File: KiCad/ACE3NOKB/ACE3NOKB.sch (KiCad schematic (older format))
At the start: 92 parts, among them J5 Conn_01x08_Female, J6 Conn_01x05_Female, J7 Conn_01x03, J8 Conn_02x05, Q1 2N3904, Q101 2N3904, Q2 2N2369, X1 6.5MHz

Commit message: Semi Complete KEyboard interface.
Signed-off-by: John Bradley <flypie@rocketmail.com>
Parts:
- Z0: Manufacturer_Part_Number Z84C0020PEG -> Z84C0020VEG
- Z101: value SN74ALS21AN -> SN74AS21N; Manufacturer_Part_Number SN74ALS21AN -> SN74AS21N
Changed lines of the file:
@@
 F 3 "" H 2925 7025 50  0001 C CNN
 F 4 "Zilog" H 400 525 50  0001 C CNN "Manufacturer_Name"
-F 5 "Z84C0020PEG" H 400 525 50  0001 C CNN "Manufacturer_Part_Number"
+F 5 "Z84C0020VEG" H 400 525 50  0001 C CNN "Manufacturer_Part_Number"
 	1    2925 6875
 	1    0    0    -1
@@
 P 11475 15275
 F 0 "Z101" H 11750 15325 50  0000 L CNN
-F 1 "SN74ALS21AN" H 11750 15275 50  0000 L CNN
+F 1 "SN74AS21N" H 11750 15275 50  0000 L CNN
 F 2 "Package_DIP:DIP-14_W7.62mm" H 11475 15275 50  0001 C CNN
 F 3 "http://www.ti.com/lit/gpn/sn74LS21" H 11475 15275 50  0001 C CNN
-F 4 "SN74ALS21AN " H 11475 15275 50  0001 C CNN "Manufacturer_Part_Number"
+F 4 "SN74AS21N" H 11475 15275 50  0001 C CNN "Manufacturer_Part_Number"
 F 5 "Texas Instruments" H 11475 15275 50  0001 C CNN "Manufacturer_Name"
 	3    11475 15275
@@
 P 6750 6075
 F 0 "Z101" H 6750 6475 50  0000 C CNN
-F 1 "SN74ALS21AN" H 6750 6375 50  0000 C CNN
+F 1 "SN74AS21N" H 6750 6375 50  0000 C CNN
 F 2 "Package_DIP:DIP-14_W7.62mm" H 6750 6075 50  0001 C CNN
 F 3 "http://www.ti.com/lit/gpn/sn74LS21" H 6750 6075 50  0001 C CNN
-F 4 "SN74ALS21AN " H 6750 6075 50  0001 C CNN "Manufacturer_Part_Number"
+F 4 "SN74AS21N" H 6750 6075 50  0001 C CNN "Manufacturer_Part_Number"
 F 5 "Texas Instruments" H 6750 6075 50  0001 C CNN "Manufacturer_Name"
 	2    6750 6075
@@
 P 5950 5775
 F 0 "Z101" H 5975 6175 50  0000 C CNN
-F 1 "SN74ALS21AN" H 5975 6075 50  0000 C CNN
+F 1 "SN74AS21N" H 5975 6075 50  0000 C CNN
 F 2 "Package_DIP:DIP-14_W7.62mm" H 5950 5775 50  0001 C CNN
 F 3 "http://www.ti.com/lit/gpn/sn74LS21" H 5950 5775 50  0001 C CNN
-F 4 "SN74ALS21AN " H 5950 5775 50  0001 C CNN "Manufacturer_Part_Number"
+F 4 "SN74AS21N" H 5950 5775 50  0001 C CNN "Manufacturer_Part_Number"
 F 5 "Texas Instruments" H 5950 5775 50  0001 C CNN "Manufacturer_Name"
 	1    5950 5775

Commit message: Latest changes fix Diode misake in 2NOKB.
Signed-off-by: John Bradley <flypie@rocketmail.com>
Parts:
- AUDIO-IN1, COMPOSITE1: Manufacturer_Name SAMTEC -> TE Connectivity / AMP; Manufacturer_Part_Number TSW–101–10–T–D–RA -> 5-146871-1
- Z80CPUOUT1: Manufacturer_Name SAMTEC -> HARWIN; Manufacturer_Part_Number TSW-122-10-T-S -> M20-9721146
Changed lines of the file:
@@
 F 2 "Connector_PinHeader_2.54mm:PinHeader_2x22_P2.54mm_Vertical" H 1300 2225 50  0001 C CNN
 F 3 "" H 1300 2225 50  0001 C CNN
-F 4 "SAMTEC" H 1300 2225 50  0001 C CNN "Manufacturer_Name"
-F 5 "TSW-122-10-T-S" H 1300 2225 50  0001 C CNN "Manufacturer_Part_Number"
+F 4 "HARWIN" H 1300 2225 50  0001 C CNN "Manufacturer_Name"
+F 5 "M20-9721146 " H 1300 2225 50  0001 C CNN "Manufacturer_Part_Number"
 	1    1300 2225
 	1    0    0    -1
@@
 F 2 "Connector_PinHeader_2.54mm:PinHeader_1x02_P2.54mm_Vertical" H 12795 3875 50  0001 C CNN
 F 3 "" H 12795 3875 50  0001 C CNN
-F 4 "SAMTEC" H 12795 3875 50  0001 C CNN "Manufacturer_Name"
-F 5 "TSW–101–10–T–D–RA" H 12795 3875 50  0001 C CNN "Manufacturer_Part_Number"
+F 4 "TE Connectivity / AMP" H 12795 3875 50  0001 C CNN "Manufacturer_Name"
+F 5 "5-146871-1" H 12795 3875 50  0001 C CNN "Manufacturer_Part_Number"
 	1    12795 3875
 	-1   0    0    -1
@@
 F 2 "Connector_PinHeader_2.54mm:PinHeader_1x02_P2.54mm_Vertical" H 20675 2200 50  0001 C CNN
 F 3 "" H 20675 2200 50  0001 C CNN
-F 4 "SAMTEC" H 20675 2200 50  0001 C CNN "Manufacturer_Name"
-F 5 "TSW–101–10–T–D–RA" H 20675 2200 50  0001 C CNN "Manufacturer_Part_Number"
+F 4 "TE Connectivity / AMP" H 20675 2200 50  0001 C CNN "Manufacturer_Name"
+F 5 "5-146871-1" H 20675 2200 50  0001 C CNN "Manufacturer_Part_Number"
 	1    20675 2200
 	1    0    0    1

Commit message: Changed component spacing for easier soldering.
Signed-off-by: John Bradley <flypie@rocketmail.com>
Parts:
- J5: footprint Connector_PinSocket_1.27mm:PinSocket_1x08_P1.27mm_Vertical -> Connector_PinSocket_2.54mm:PinSocket_1x08_P2.54mm_Vertical
- J6: footprint Connector_PinSocket_1.27mm:PinSocket_1x05_P1.27mm_Vertical -> Connector_PinSocket_2.54mm:PinSocket_1x05_P2.54mm_Vertical
- J7: footprint Connector_PinHeader_1.27mm:PinHeader_1x03_P1.27mm_Vertical -> Connector_PinHeader_2.54mm:PinHeader_1x03_P2.54mm_Vertical
- J8: footprint Connector_PinHeader_1.27mm:PinHeader_2x05_P1.27mm_Vertical -> Connector_PinHeader_2.54mm:PinHeader_2x05_P2.54mm_Vertical
- Q1, Q101: footprint Package_TO_SOT_THT:TO-92_Inline -> Package_TO_SOT_THT:TO-92_Inline_Wide
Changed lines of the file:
@@
 F 0 "J8" H 17600 9725 50  0000 C CNN
 F 1 "Conn_02x05" H 17600 9625 50  0000 C CNN
-F 2 "Connector_PinHeader_1.27mm:PinHeader_2x05_P1.27mm_Vertical" H 17525 9275 50  0001 C CNN
+F 2 "Connector_PinHeader_2.54mm:PinHeader_2x05_P2.54mm_Vertical" H 17525 9275 50  0001 C CNN
 F 3 "" H 17525 9275 50  0001 C CNN
 F 4 "HARWIN" H 17525 9275 50  0001 C CNN "Manufacturer_Name"
@@
 F 0 "J7" H 18250 9550 50  0000 C CNN
 F 1 "Conn_01x03" H 18250 9450 50  0000 C CNN
-F 2 "Connector_PinHeader_1.27mm:PinHeader_1x03_P1.27mm_Vertical" H 18375 9175 50  0001 C CNN
+F 2 "Connector_PinHeader_2.54mm:PinHeader_1x03_P2.54mm_Vertical" H 18375 9175 50  0001 C CNN
 F 3 "" H 18375 9175 50  0001 C CNN
 F 4 "HARWIN" H 18375 9175 50  0001 C CNN "Manufacturer_Name"
@@
 F 0 "J6" H 18075 10350 50  0000 C CNN
 F 1 "Conn_01x05_Female" H 18075 10250 50  0000 C CNN
-F 2 "Connector_PinSocket_1.27mm:PinSocket_1x05_P1.27mm_Vertical" H 18200 9925 50  0001 C CNN
+F 2 "Connector_PinSocket_2.54mm:PinSocket_1x05_P2.54mm_Vertical" H 18200 9925 50  0001 C CNN
 F 3 "" H 18200 9925 50  0001 C CNN
 F 4 "HARWIN" H 18200 9925 50  0001 C CNN "Manufacturer_Name"
@@
 F 0 "J5" H 17700 10025 50  0000 L CNN
 F 1 "Conn_01x08_Female" H 17700 9925 50  0000 L CNN
-F 2 "Connector_PinSocket_1.27mm:PinSocket_1x08_P1.27mm_Vertical" H 17625 10025 50  0001 C CNN
+F 2 "Connector_PinSocket_2.54mm:PinSocket_1x08_P2.54mm_Vertical" H 17625 10025 50  0001 C CNN
 F 3 "" H 17625 10025 50  0001 C CNN
 F 4 "HARWIN" H 17625 10025 50  0001 C CNN "Manufacturer_Name"
@@
 F 0 "Q1" H 14050 9875 50  0000 L CNN
 F 1 "2N3904" H 13625 9675 50  0000 L CNN
-F 2 "Package_TO_SOT_THT:TO-92_Inline" H 14050 9750 50  0001 L CIN
+F 2 "Package_TO_SOT_THT:TO-92_Inline_Wide" H 14050 9750 50  0001 L CIN
 F 3 "" H 13850 9825 50  0001 L CNN
 F 4 "2N3904" H 13850 9825 50  0001 C CNN "Manufacturer_Part_Number"
@@
 F 0 "Q101" H 20300 2175 50  0000 L CNN
 F 1 "2N3904" H 20300 2075 50  0000 L CNN
-F 2 "Package_TO_SOT_THT:TO-92_Inline" H 20075 2100 50  0001 C CNN
+F 2 "Package_TO_SOT_THT:TO-92_Inline_Wide" H 20075 2100 50  0001 C CNN
 F 3 "" H 20075 2100 50  0001 C CNN
 F 4 "2N3904" H 20075 2100 50  0001 C CNN "Manufacturer_Part_Number"

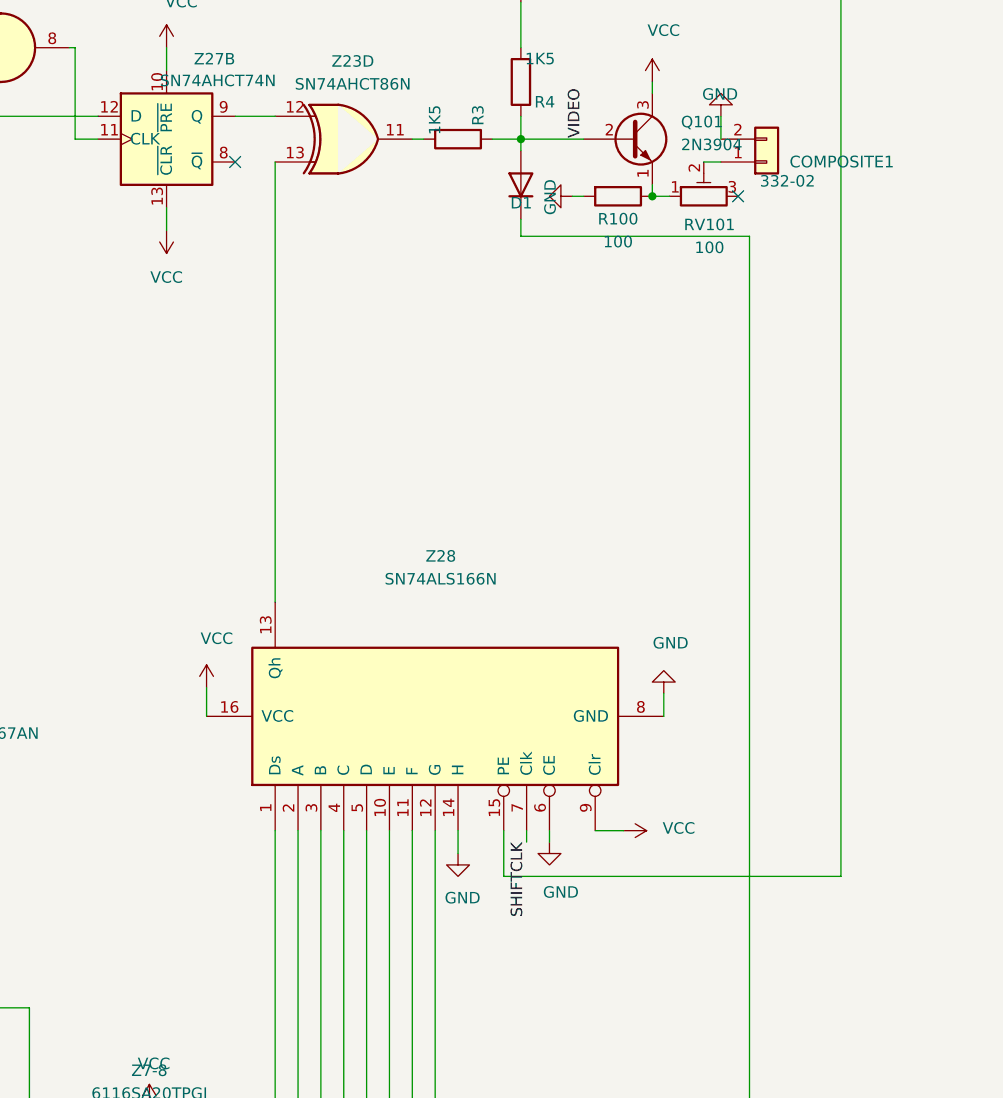
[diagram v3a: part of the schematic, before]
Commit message: Correct proble with prins connected to Parrlel to serial shifter.
Signed-off-by: John Bradley <flypie@rocketmail.com>
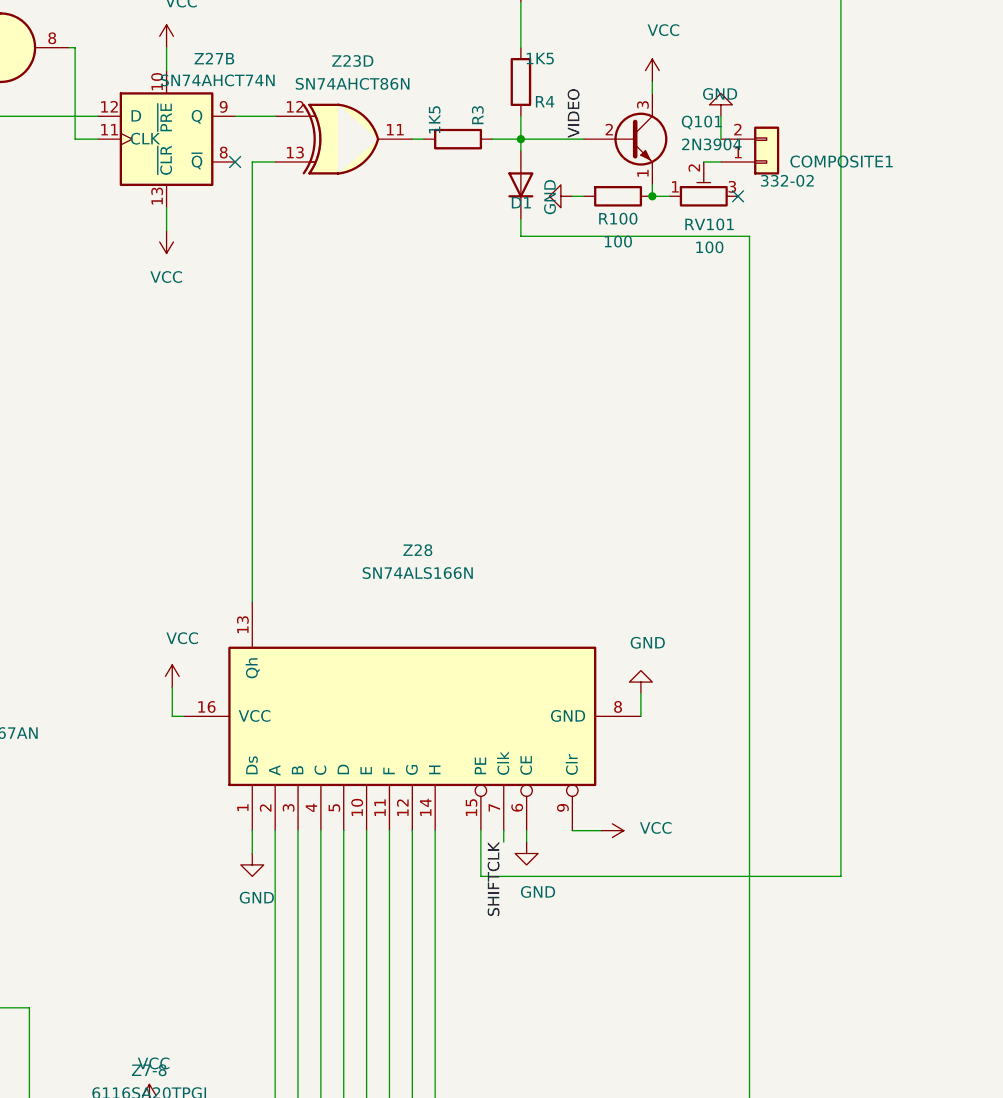
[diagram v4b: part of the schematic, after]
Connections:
- net GND: now also Z28.1 (Ds); no longer Z28.14 (H)
- net at RN2.15 (R2.2), Z7-8.10 (D1): now also Z28.3 (B); no longer Z28.2 (A)
- net at RN2.14 (R3.2), Z7-8.11 (D2): now also Z28.4 (C); no longer Z28.3 (B)
- net at RN2.13 (R4.2), Z7-8.13 (D3): now also Z28.5 (D); no longer Z28.4 (C)
- net at RN2.12 (R5.2), Z7-8.14 (D4): now also Z28.10 (E); no longer Z28.5 (D)
- net at RN2.11 (R6.2), Z7-8.15 (D5): now also Z28.11 (F); no longer Z28.10 (E)
- net at RN2.10 (R7.2), Z7-8.16 (D6): now also Z28.12 (G); no longer Z28.11 (F)
- net at RN2.9 (R8.2), Z7-8.17 (D7): now also Z28.14 (H); no longer Z28.12 (G)
- net at RN2.16 (R1.2), Z7-8.9 (D0): now also Z28.2 (A); no longer Z28.1 (Ds)
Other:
- moved on the sheet: Z28
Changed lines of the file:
@@
 $EndComp
 $Comp
-L power:GND #~PWR0113
-U 1 1 690A98BA
-P 20225 4525
-F 0 "#~PWR0113" H 20225 4275 50  0001 C CNN
-F 1 "GND" H 20195 4305 50  0000 C CNN
-F 2 "" H 20225 4525 50  0001 C CNN
-F 3 "" H 20225 4525 50  0001 C CNN
-	1    20225 4525
-	-1   0    0    1
-$EndComp
-$Comp
 L power:VCC #~PWR0111
 U 1 1 68CB052C
-P 18225 4500
-F 0 "#~PWR0111" H 18225 4350 50  0001 C CNN
-F 1 "VCC" H 18270 4715 50  0000 C CNN
-F 2 "" H 18225 4500 50  0001 C CNN
-F 3 "" H 18225 4500 50  0001 C CNN
-	1    18225 4500
+P 18075 4500
+F 0 "#~PWR0111" H 18075 4350 50  0001 C CNN
+F 1 "VCC" H 18120 4715 50  0000 C CNN
+F 2 "" H 18075 4500 50  0001 C CNN
+F 3 "" H 18075 4500 50  0001 C CNN
+	1    18075 4500
 	1    0    0    -1
 $EndComp
@@
 	7000 4300 7000 3500
 Wire Wire Line
-	19325 5125 19325 5225
+	18425 5125 18425 5225
 $Comp
 L power:GND #~PWR0126
 U 1 1 68217D27
-P 19325 5225
-F 0 "#~PWR0126" H 19325 4975 50  0001 C CNN
-F 1 "GND" H 19345 5030 50  0000 C CNN
-F 2 "" H 19325 5225 50  0001 C CNN
-F 3 "" H 19325 5225 50  0001 C CNN
-	1    19325 5225
+P 18425 5225
+F 0 "#~PWR0126" H 18425 4975 50  0001 C CNN
+F 1 "GND" H 18445 5030 50  0000 C CNN
+F 2 "" H 18425 5225 50  0001 C CNN
+F 3 "" H 18425 5225 50  0001 C CNN
+	1    18425 5225
 	1    0    0    -1
 $EndComp
@@
 Wire Wire Line
 	17975 6400 17975 6335
-$Comp
-L power:VCC #~PWR0125
-U 1 1 682088BB
-P 20050 5125
-F 0 "#~PWR0125" H 20050 4975 50  0001 C CNN
-F 1 "VCC" V 20040 5295 50  0000 L CNN
-F 2 "" H 20050 5125 50  0001 C CNN
-F 3 "" H 20050 5125 50  0001 C CNN
-	1    20050 5125
-	0    1    1    0
-$EndComp
-Wire Wire Line
-	20225 4525 20225 4625
-Wire Wire Line
-	19925 5125 20050 5125
 Wire Wire Line
-	18225 4625 18225 4500
+	18075 4625 18075 4500
 Wire Wire Line
 	18825 5125 18825 7000
@@
 ~MREQ
 Wire Wire Line
-	19525 5325 19525 5125
-Wire Wire Line
 	2200 9100 2200 9000
 Wire Wire Line
@@
 $EndComp
 $Comp
-L 74xx:74LS166 Z28
-U 1 1 6FFDAE7B
-P 19225 4625
-F 0 "Z28" V 19925 4600 50  0000 C CNN
-F 1 "SN74ALS166N" V 19825 4600 50  0000 C CNN
-F 2 "Package_DIP:DIP-16_W7.62mm" H 19225 4625 50  0001 C CNN
-F 3 "http://www.ti.com/lit/gpn/sn74LS166" H 19225 4625 50  0001 C CNN
-F 4 "SN74ALS166N" H 19225 4625 50  0001 C CNN "Manufacturer_Part_Number"
-F 5 "Texas Instruments" H 19225 4625 50  0001 C CNN "Manufacturer_Name"
-F 6 "595-SN74ALS166N" H 19225 4625 50  0001 C CNN "Allied_Number"
-	1    19225 4625
-	0    -1   -1   0
-$EndComp
-$Comp
 L Device:R R21
 U 1 1 8FE8240F
@@
 $EndComp
 Wire Wire Line
-	18525 2200 18525 4125
-Wire Wire Line
 	15150 1900 15175 1900
 Wire Wire Line
@@
 	21000 1000 21000 5325
 Wire Wire Line
-	19525 5325 21000 5325
-$Comp
-L power:GND #~PWR0127
-U 1 1 68218186
-P 19725 5175
-F 0 "#~PWR0127" H 19725 4925 50  0001 C CNN
-F 1 "GND" H 19775 4955 50  0000 C CNN
-F 2 "" H 19725 5175 50  0001 C CNN
-F 3 "" H 19725 5175 50  0001 C CNN
-	1    19725 5175
-	1    0    0    -1
-$EndComp
-Wire Wire Line
-	19725 5125 19725 5175
-Wire Wire Line
-	19625 5125 19625 5175
-Text Label 19625 5175 3    50   ~ 0
-SHIFTCLK
-Wire Wire Line
 	15850 2100 15850 2700
 Wire Wire Line
@@
 Wire Wire Line
 	15850 1100 17675 1100
+Text Label 19525 5175 3    50   ~ 0
+SHIFTCLK
+Wire Wire Line
+	19525 5125 19525 5175
+Wire Wire Line
+	19625 5125 19625 5175
+$Comp
+L power:GND #~PWR0127
+U 1 1 68218186
+P 19625 5175
+F 0 "#~PWR0127" H 19625 4925 50  0001 C CNN
+F 1 "GND" H 19675 4955 50  0000 C CNN
+F 2 "" H 19625 5175 50  0001 C CNN
+F 3 "" H 19625 5175 50  0001 C CNN
+	1    19625 5175
+	1    0    0    -1
+$EndComp
+$Comp
+L 74xx:74LS166 Z28
+U 1 1 6FFDAE7B
+P 19125 4625
+F 0 "Z28" V 19850 4600 50  0000 C CNN
+F 1 "SN74ALS166N" V 19750 4600 50  0000 C CNN
+F 2 "Package_DIP:DIP-16_W7.62mm" H 19125 4625 50  0001 C CNN
+F 3 "http://www.ti.com/lit/gpn/sn74LS166" H 19125 4625 50  0001 C CNN
+F 4 "SN74ALS166N" H 19125 4625 50  0001 C CNN "Manufacturer_Part_Number"
+F 5 "Texas Instruments" H 19125 4625 50  0001 C CNN "Manufacturer_Name"
+F 6 "595-SN74ALS166N" H 19125 4625 50  0001 C CNN "Allied_Number"
+	1    19125 4625
+	0    -1   -1   0
+$EndComp
+Wire Wire Line
+	19425 5325 19425 5125
+Wire Wire Line
+	19825 5125 19950 5125
+Wire Wire Line
+	20125 4525 20125 4625
+$Comp
+L power:VCC #~PWR0125
+U 1 1 682088BB
+P 19950 5125
+F 0 "#~PWR0125" H 19950 4975 50  0001 C CNN
+F 1 "VCC" V 19940 5295 50  0000 L CNN
+F 2 "" H 19950 5125 50  0001 C CNN
+F 3 "" H 19950 5125 50  0001 C CNN
+	1    19950 5125
+	0    1    1    0
+$EndComp
+$Comp
+L power:GND #~PWR0113
+U 1 1 690A98BA
+P 20125 4525
+F 0 "#~PWR0113" H 20125 4275 50  0001 C CNN
+F 1 "GND" H 20095 4305 50  0000 C CNN
+F 2 "" H 20125 4525 50  0001 C CNN
+F 3 "" H 20125 4525 50  0001 C CNN
+	1    20125 4525
+	-1   0    0    1
+$EndComp
+Wire Wire Line
+	18125 4625 18075 4625
+Wire Wire Line
+	18425 4125 18425 2200
+Wire Wire Line
+	18425 2200 18525 2200
+Wire Wire Line
+	19425 5325 21000 5325
 $EndSCHEMATC

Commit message: The V 0 of the ACE3NOKB was duff. First attempt at fixing, plus revided ROM scheme and some bigger pin spacing.
Signed-off-by: John Bradley <flypie@rocketmail.com>
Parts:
- removed Z10, Z11, Z9: CD74HCT393E, Package_DIP:DIP-14_W7.62mm, symbol 74xx:74LS393
- added R130, R131: 10k, Resistor_THT:R_Axial_DIN0204_L3.6mm_D1.6mm_P1.90mm_Vertical, symbol Device:R
- added R132, R133, R134, R135: 1K, Resistor_THT:R_Axial_DIN0204_L3.6mm_D1.6mm_P1.90mm_Vertical, symbol Device:R
- added R136: 10K, Resistor_THT:R_Axial_DIN0204_L3.6mm_D1.6mm_P1.90mm_Vertical, symbol Device:R
- added Z360: SN74AHCT08N, Package_DIP:DIP-14_W7.62mm, symbol 74xx:74LS08
- J5: value Conn_01x08_Female -> Conn_01x12_Female; footprint Connector_PinSocket_2.54mm:PinSocket_1x08_P2.54mm_Vertical -> Connector_PinSocket_2.54mm:PinSocket_1x12_P2.54mm_Vertical; symbol Connector:Conn_01x08_Female -> Connector:Conn_01x12_Female
- J6: value Conn_01x05_Female -> Conn_01x09_Female; footprint Connector_PinSocket_2.54mm:PinSocket_1x05_P2.54mm_Vertical -> Connector_PinSocket_2.54mm:PinSocket_1x09_P2.54mm_Vertical; symbol Connector:Conn_01x05_Female -> Connector:Conn_01x09_Female
- R110: value 270R -> 10k; Manufacturer_Part_Number MBA02040C2700FRP00 -> MBA02040C1002FRP00
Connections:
- net A10: now also Z19.13, Z25.9
- net A12: no longer Z26.4
- net EOL: now also J6.9 (Pin_9)
- net GND: now also R132.2, R133.2, R134.1, R135.1, Z360.7 (GND); no longer Z28.1 (Ds), Z28.6 (CE), Z5-6.19 (A10), Z7-8.19 (A10)
- net SCREENX2: now also J6.6 (Pin_6)
- net SCREENX3: now also J6.7 (Pin_7)
- net SCREENX4: now also J6.8 (Pin_8)
- net VIDEN: now also Z20.12, Z20.6; no longer Z20.9, Z22.6
- net ~INT: now also R130.2
- net ~RD: now also Z26.10
- net ~WAIT: now also R131.2
- net ~WR: now also Z26.5
- net ~BOTTOM32K: now reaches Z101.6, Z3-4.20 (~CE)
- net XRESET: now reaches Z21.8
- net YRESET: now reaches Z20.3
- net at Z1-2.22 (CE), Z1-2.24 (OE): now also Z101.8; no longer Z22.8
- net ~3C00-3FFF: now reaches Z19.11
- net ~3C00-3FFF: now also Z101.1
- net at Z19.12: now also Z102.10
- net BASECLK_DIV_2: now reaches J5.1 (Pin_1), J8.3 (Pin_3)
- net BASECLK_DIV_4: now reaches J5.2 (Pin_2), J8.5 (Pin_5)
- net BASECLK_DIV_8: now reaches J5.3 (Pin_3), J8.7 (Pin_7)
- net BASECLK_DIV_16: now reaches J5.4 (Pin_4), J8.9 (Pin_9)
- net BASECLK_DIV_32: now reaches J5.5 (Pin_5)
- net BASECLK_DIV_64: now reaches J5.6 (Pin_6)
- net BASECLK_DIV_128: now reaches J5.7 (Pin_7)
- net BASECLK_DIV_256: now reaches J5.8 (Pin_8)
- net ~CPUVDGRAMWR: now reaches R32.2, Z102.3, Z26.11, Z5-6.21 (~WE), Z7-8.21 (~WE)
- net ~CPUVDGRAMRD: now reaches Z102.4, Z5-6.20 (~OE), Z7-8.20 (~OE)
- net at Z22.9: now also Z29.10 (O5); no longer Z111.10 (O2)
- net at Z111.15 (E), Z29.14 (O1): no longer Z26.5
- net at Z22.10: now also Z29.9 (O6); no longer Z111.9 (O3)
- net at Z29.13 (O2): now also Z101.2; no longer Z101.1
- net at Z29.12 (O3): now also Z101.4; no longer Z101.2
- net at Z29.11 (O4): now also Z101.5; no longer Z101.4
- net ~TOP32K: now reaches Z120.20 (~CE)
- net ~TOP32K: now also Z22.8; no longer Z101.8
- net ~CPUINVDGRAM: now reaches Z102.1
- net ~CPUINVDGRAM: now also R26.2, Z26.2, Z360.3
- net CPUINVDGRAM: now reaches Z102.2
- net CPUINVDGRAM: now also Z360.5, Z360.9
- net ~3800-3FFF: now reaches Z102.11
- net ~3800-3FFF: now also Z111.9 (O3), Z25.8
- net at Z22.11: now also Z29.7 (O7); no longer Z29.15 (O0)
- net ~CPUCSCHARROM: now reaches Z26.8
- net ~CPUCSCHARROM: now also Z101.12
- net ~CPUCSCHAR: now reaches Z26.9
- net ~CPUCSCHAR: now also Z111.11 (O1), Z26.4
- net ~3800-3BFF: now reaches Z25.10
- net ~3800-3BFF: now also Z101.9
- net +5V renamed VCC
- net VCC: now also R130.1, R131.1, R136.1, Z360.14 (VCC); no longer Z28.9 (Clr)
- net CLK\TRG3 renamed 50Hz
- net ~CSCS renamed ~CSCHARRAM
- net ~CSCHARRAM: now also Z360.6; no longer Z111.12 (O0)
- net ~CSSB renamed ~CSVIDEORAM
- net ~CSVIDEORAM: now also Z360.8; no longer Z111.11 (O1)
- new net: R133.1, Z7-8.19 (A10)
- new net: Z19.5, Z20.9, Z22.6
- new net: R132.1, Z5-6.19 (A10)
- new net: R134.2, Z28.1 (Ds)
- new net: R135.2, Z28.6 (CE)
- new net: R136.2, Z28.9 (Clr)
- new net 0000-1FFF: Z101.13, Z29.15 (O0)
- new net BASECLK_DIV_1024: J5.10 (Pin_10)
- new net BASECLK_DIV_2048: J5.11 (Pin_11)
- new net BASECLK_DIV_4096: J5.12 (Pin_12)
- new net BASECLK_DIV_512: J5.9 (Pin_9)
- new net ~3000-37FF: Z101.10, Z111.10 (O2)
- new net ~CPUCSCHARRAM: Z26.6, Z360.1, Z360.4
- new net ~CPUCSVIDEORAM: Z111.12 (O0), Z360.10, Z360.2
- no-connect marks 31 -> 18
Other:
- note removed: "Produce an OE by inverting WR"
- moved on the sheet: AUDIO-IN1, C1, C10, C11, C12, C13, C14, C15, C16, C17, C18, C19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

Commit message: Some more tidying up of V0.1.
Signed-off-by: John Bradley <flypie@rocketmail.com>
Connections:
- net VCC: no longer Z16.12 (I5)
- no-connect marks 18 -> 19
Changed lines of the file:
@@
 	9815 8550 9875 8550
 Wire Wire Line
-	9875 8450 9755 8450
-$Comp
-L power:VCC #~PWR0143
-U 1 1 6EE1F51B
-P 9755 8450
-F 0 "#~PWR0143" H 9755 8300 50  0001 C CNN
-F 1 "VCC" V 9795 8585 50  0000 L CNN
-F 2 "" H 9755 8450 50  0001 C CNN
-F 3 "" H 9755 8450 50  0001 C CNN
-	1    9755 8450
-	0    -1   -1   0
-$EndComp
+	9875 8450 9825 8450
 Wire Wire Line
 	17225 2450 17225 6250
@@
 U 5 1 60FCF032
 P 2725 4075
-F 0 "Z102" H 2725 4450 50  0000 C CNN
-F 1 "SN74AHCT04N" H 2725 4350 50  0000 C CNN
+F 0 "Z102" H 2750 4450 50  0000 C CNN
+F 1 "SN74AHCT04N" H 2750 4350 50  0000 C CNN
 F 2 "Package_DIP:DIP-14_W7.62mm" H 2725 4075 50  0001 C CNN
 F 3 "http://www.ti.com/lit/gpn/snSN74AHCT04" H 2725 4075 50  0001 C CNN
@@
 Wire Wire Line
 	20325 4875 20375 4875
+NoConn ~ 9825 8450
 $EndSCHEMATC
